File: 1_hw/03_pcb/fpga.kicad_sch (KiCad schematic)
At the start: 1 part, among them U2 ICE40UP5K-SG48ITR

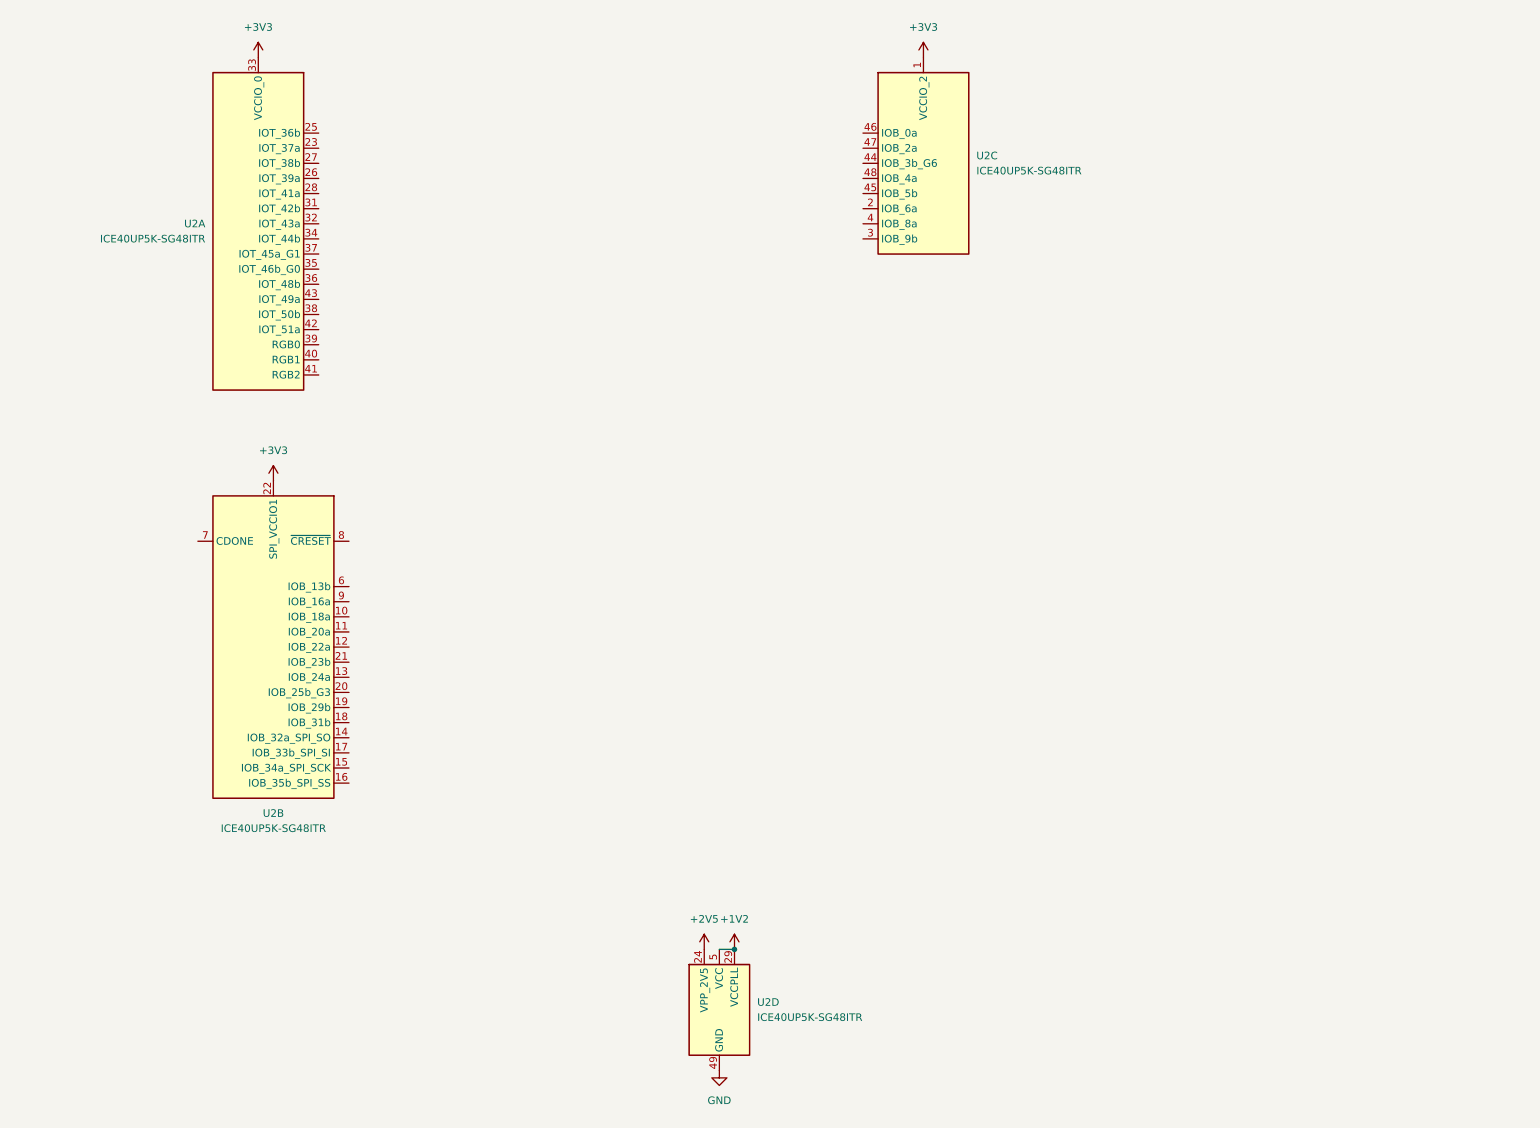
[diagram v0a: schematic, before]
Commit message: FEAT: Finished Excel Pin Map for MCU. Completed MCU + FPGA in Schematic.
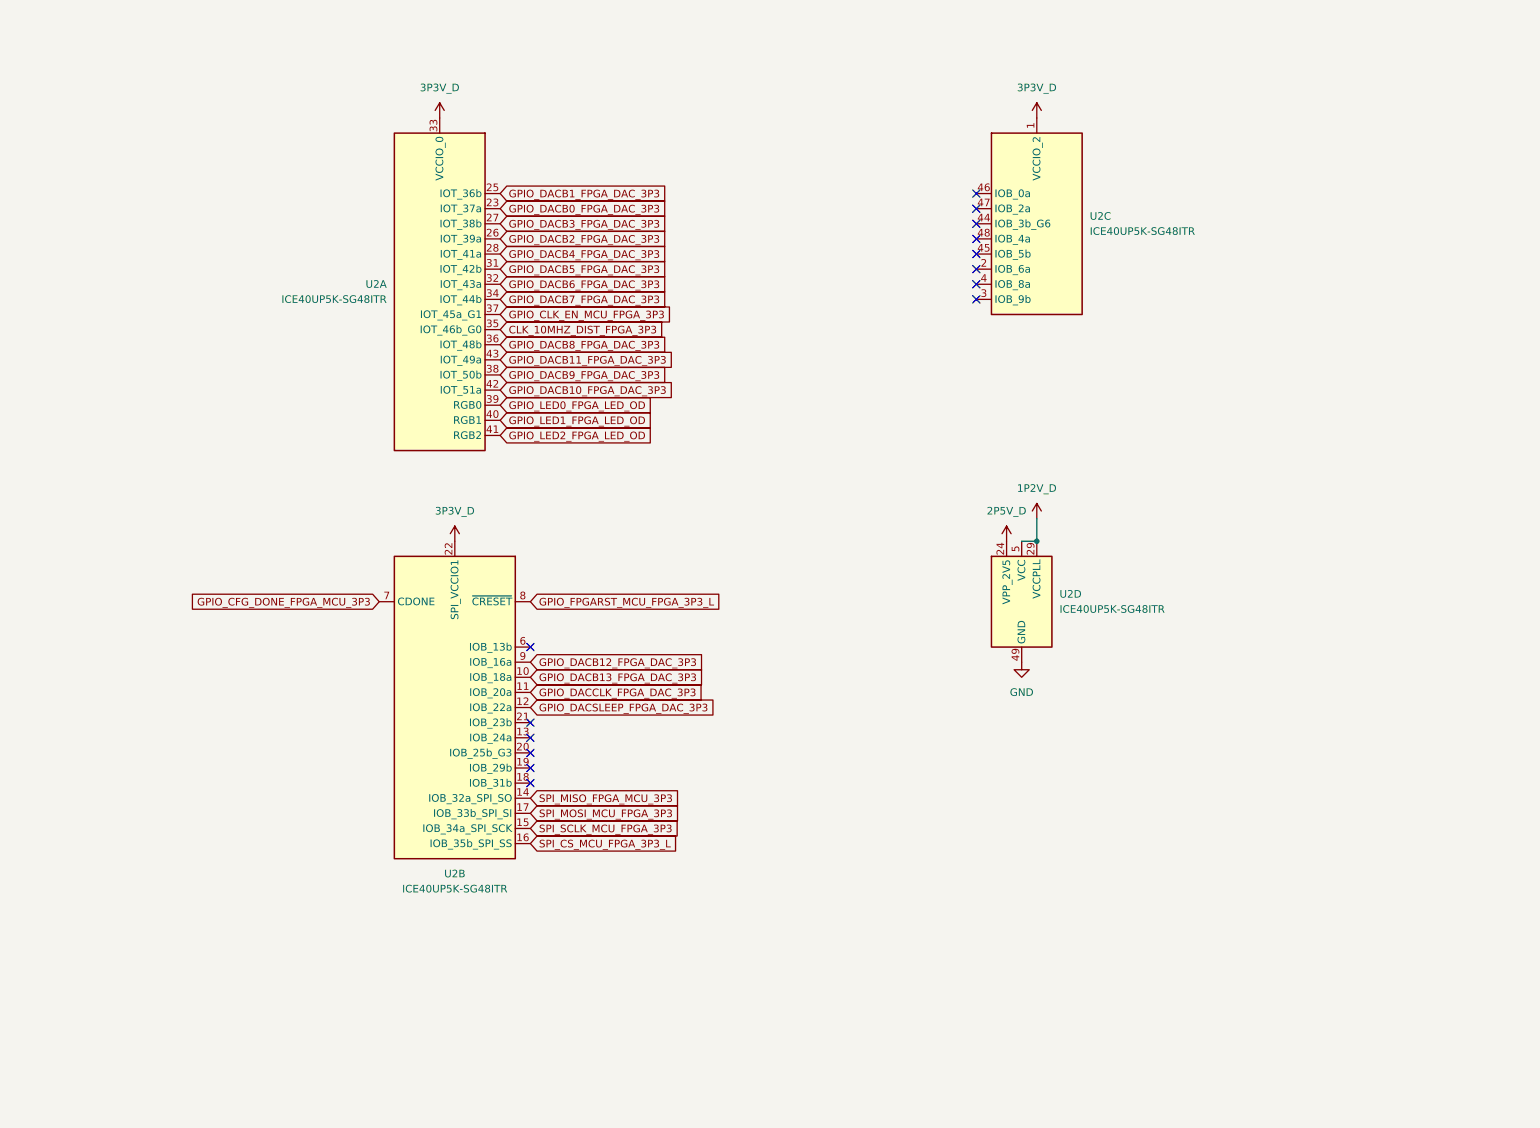
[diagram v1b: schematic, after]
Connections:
- net GPIO_DACB0_FPGA_DAC_3P3: now reaches U2.23 (IOT_37a)
- net GPIO_DACB1_FPGA_DAC_3P3: now reaches U2.25 (IOT_36b)
- net GPIO_DACB2_FPGA_DAC_3P3: now reaches U2.26 (IOT_39a)
- net GPIO_DACB3_FPGA_DAC_3P3: now reaches U2.27 (IOT_38b)
- net GPIO_DACB4_FPGA_DAC_3P3: now reaches U2.28 (IOT_41a)
- net GPIO_DACB5_FPGA_DAC_3P3: now reaches U2.31 (IOT_42b)
- net GPIO_DACB6_FPGA_DAC_3P3: now reaches U2.32 (IOT_43a)
- net GPIO_DACB7_FPGA_DAC_3P3: now reaches U2.34 (IOT_44b)
- net CLK_10MHZ_DIST_FPGA_3P3: now reaches U2.35 (IOT_46b_G0)
- net GPIO_DACB8_FPGA_DAC_3P3: now reaches U2.36 (IOT_48b)
- net GPIO_CLK_EN_MCU_FPGA_3P3: now reaches U2.37 (IOT_45a_G1)
- net GPIO_DACB9_FPGA_DAC_3P3: now reaches U2.38 (IOT_50b)
- net GPIO_LED0_FPGA_LED_OD: now reaches U2.39 (RGB0)
- net GPIO_LED1_FPGA_LED_OD: now reaches U2.40 (RGB1)
- net GPIO_LED2_FPGA_LED_OD: now reaches U2.41 (RGB2)
- net GPIO_DACB10_FPGA_DAC_3P3: now reaches U2.42 (IOT_51a)
- net GPIO_DACB11_FPGA_DAC_3P3: now reaches U2.43 (IOT_49a)
- net GPIO_DACB13_FPGA_DAC_3P3: now reaches U2.10 (IOB_18a)
- net GPIO_DACCLK_FPGA_DAC_3P3: now reaches U2.11 (IOB_20a)
- net GPIO_DACSLEEP_FPGA_DAC_3P3: now reaches U2.12 (IOB_22a)
- net SPI_MISO_FPGA_MCU_3P3: now reaches U2.14 (IOB_32a_SPI_SO)
- net SPI_SCLK_MCU_FPGA_3P3: now reaches U2.15 (IOB_34a_SPI_SCK)
- net SPI_CS_MCU_FPGA_3P3_L: now reaches U2.16 (IOB_35b_SPI_SS)
- net SPI_MOSI_MCU_FPGA_3P3: now reaches U2.17 (IOB_33b_SPI_SI)
- net GPIO_CFG_DONE_FPGA_MCU_3P3: now reaches U2.7 (CDONE)
- net GPIO_FPGARST_MCU_FPGA_3P3_L: now reaches U2.8 (~{CRESET})
- net GPIO_DACB12_FPGA_DAC_3P3: now reaches U2.9 (IOB_16a)
- net +1V2 renamed 1P2V_D
- net +2V5 renamed 2P5V_D
- net +3V3 renamed 3P3V_D
- no-connect marks 0 -> 14
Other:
- moved on the sheet: U2A, U2B, U2C, U2D

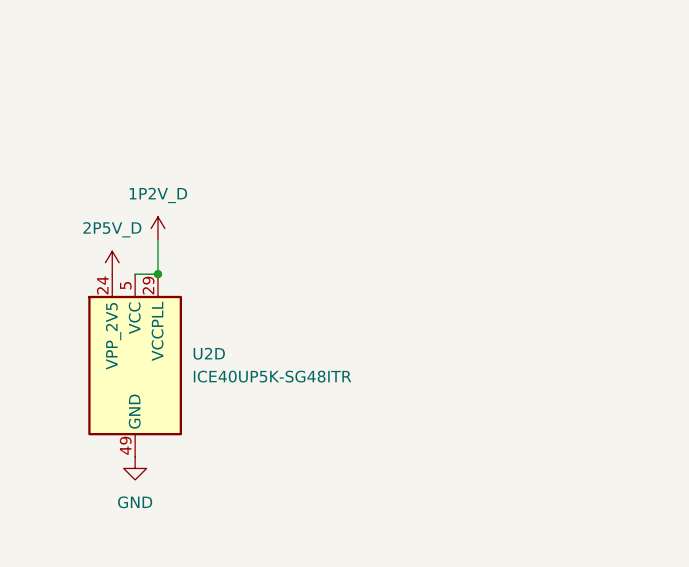
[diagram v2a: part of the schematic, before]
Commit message: FEAT: Added USB ESD Protection.
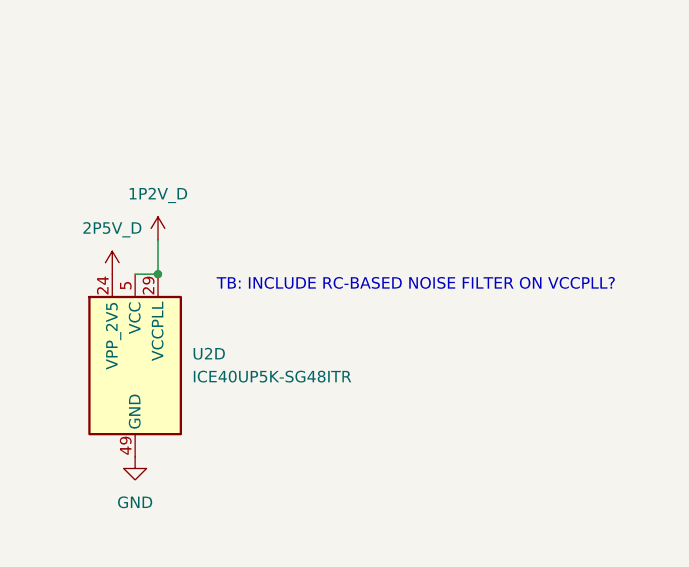
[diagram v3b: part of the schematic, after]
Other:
- note added: "TB: INCLUDE RC-BASED NOISE FILTER ON VCCPLL?"
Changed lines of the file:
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@@
+		)
+	)
+	(text "TB: INCLUDE RC-BASED NOISE FILTER ON VCCPLL?"
+		(exclude_from_sim no)
+		(at 211.582 106.68 0)
+		(effects
+			(font
+				(size 1.27 1.27)
+			)
 		)
 	)

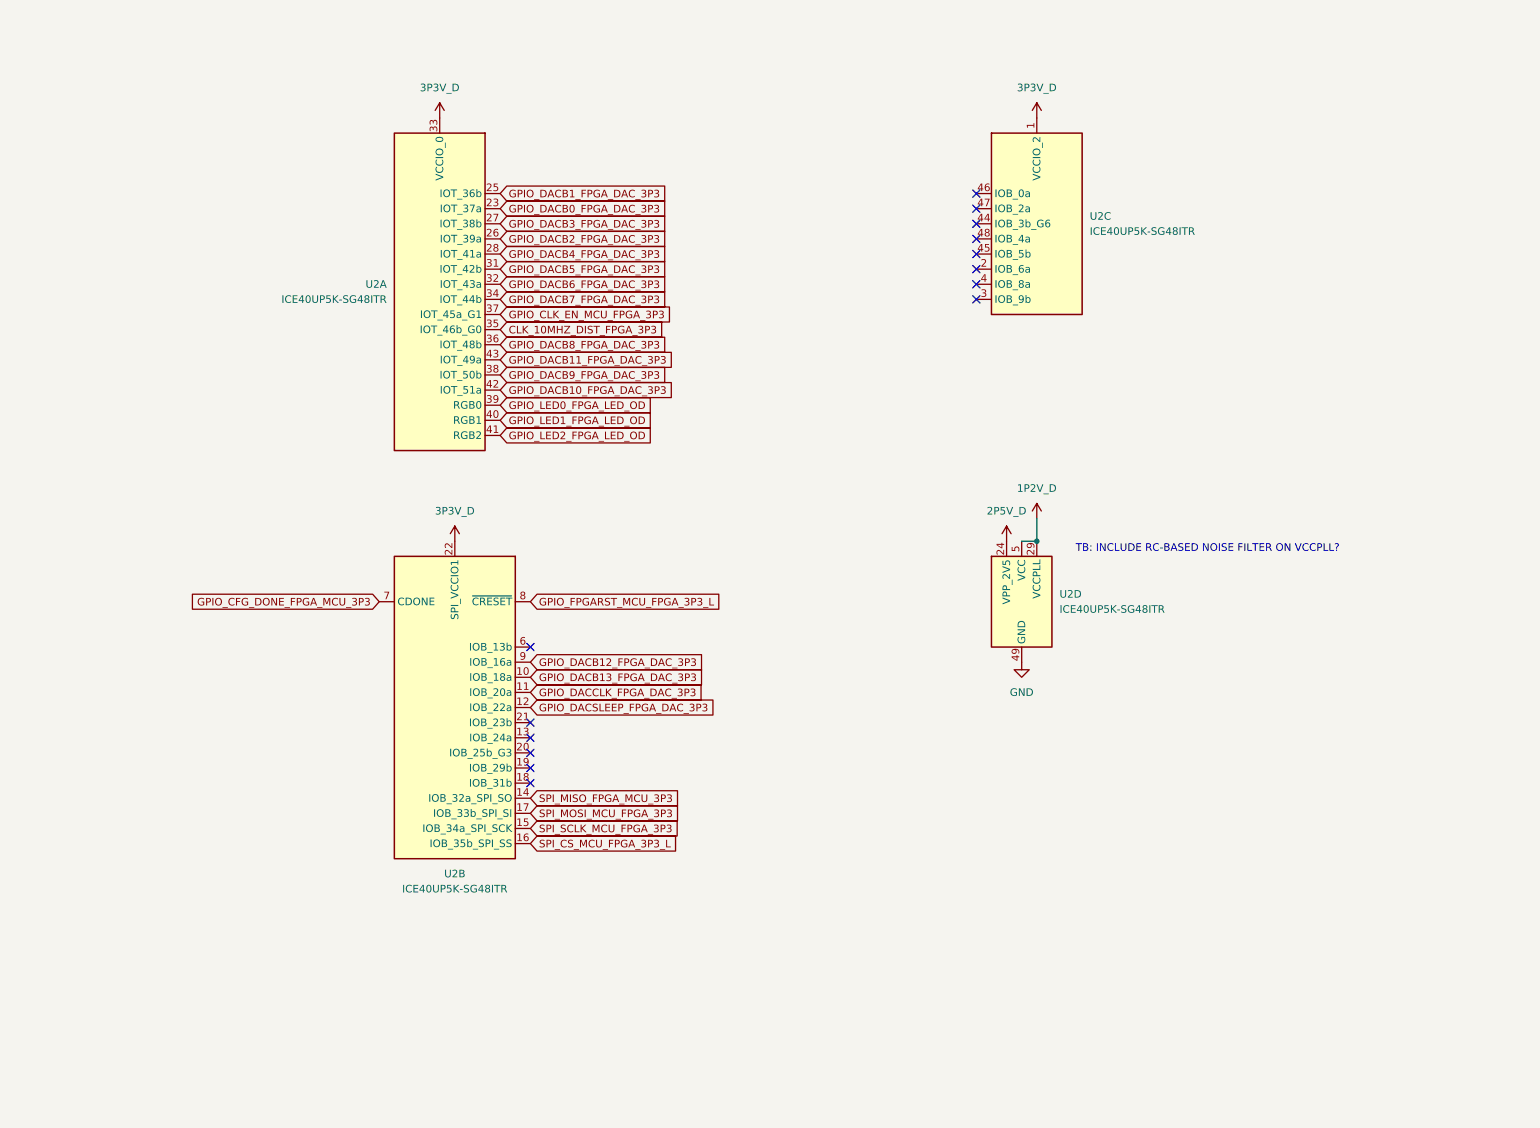
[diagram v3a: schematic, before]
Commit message: FEAT: Added Clocking Sheet, FPGA Flash, and FPGA Decoupling.
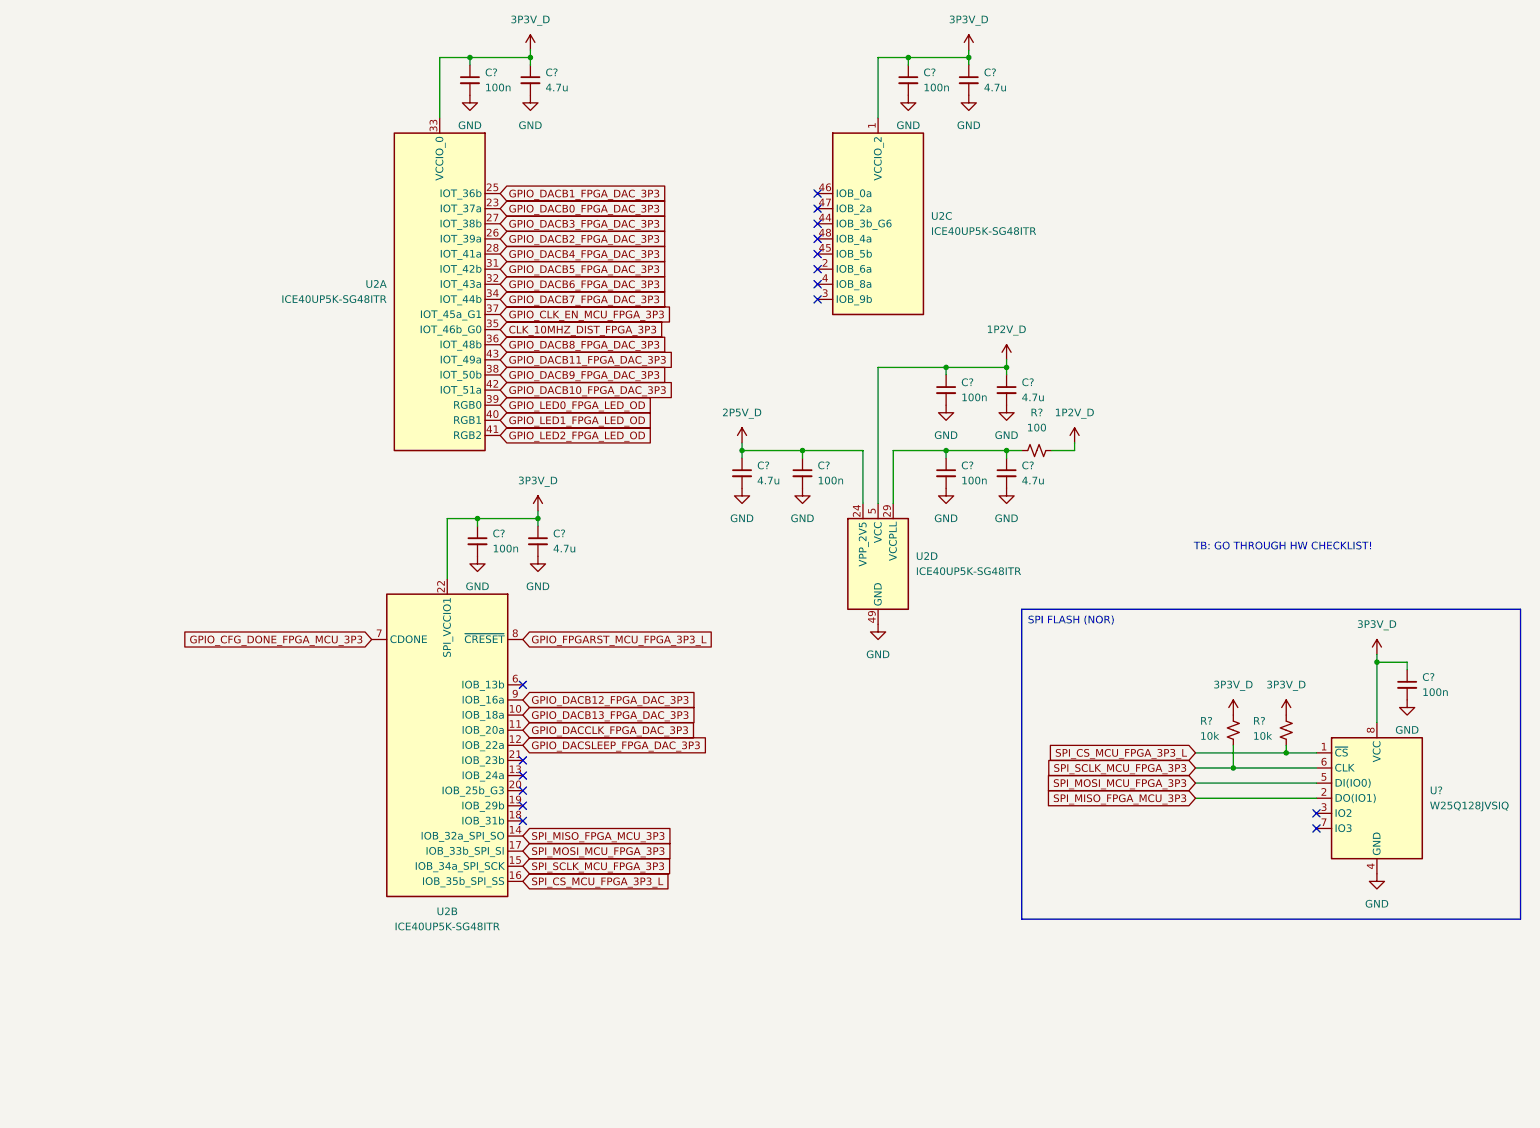
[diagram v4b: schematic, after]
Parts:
- added C? (x6): 100n, symbol Device:C_Small
- added C? (x6): 4.7u, symbol Device:C_Small
- added C?: 100n, Capacitor_SMD:C_0603_1608Metric, symbol Device:C_Small
- added R? (x2): 10k, Resistor_SMD:R_0603_1608Metric, symbol Device:R_Small_US
- added R?: 100, symbol Device:R_Small_US
- added U?: W25Q128JVSIQ, Package_SO:SOIC-8_5.23x5.23mm_P1.27mm, symbol BRZK_MEMORY:W25Q128JVSIQ
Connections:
- net 1P2V_D: now also C?.1, C?.1, R?.1; no longer U2.29 (VCCPLL)
- net 2P5V_D: now also C?.1, C?.1
- net 3P3V_D: now also C?.1, C?.1, C?.1, C?.1, C?.1, C?.1, C?.1, R?.2, R?.2, U?.8 (VCC)
- net GND: now also C?.2, C?.2, C?.2, C?.2, C?.2, C?.2, C?.2, C?.2, C?.2, C?.2, C?.2, C?.2, C?.2, U?.4 (GND)
- net SPI_CS_MCU_FPGA_3P3_L: now also R?.1, U?.1 (~{CS})
- net SPI_MISO_FPGA_MCU_3P3: now also U?.2 (DO(IO1))
- net SPI_MOSI_MCU_FPGA_3P3: now also U?.5 (DI(IO0))
- net SPI_SCLK_MCU_FPGA_3P3: now also R?.1, U?.6 (CLK)
- new net: C?.1, C?.1, R?.2, U2.29 (VCCPLL)
- no-connect marks 14 -> 16
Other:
- note added: "TB: GO THROUGH HW CHECKLIST!"
- note removed: "TB: INCLUDE RC-BASED NOISE FILTER ON VCCPLL?"
- moved on the sheet: U2B, U2C, U2D
